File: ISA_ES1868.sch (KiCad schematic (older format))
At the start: 44 parts, among them J1 ISA BUS, J1 LINE, J2 MIC, J3 Joystick/MIDI, J5 Wavetable, U1 L78L05_TO92, U2 74LS138, U4 93LC66, Y1 14.318Mhz

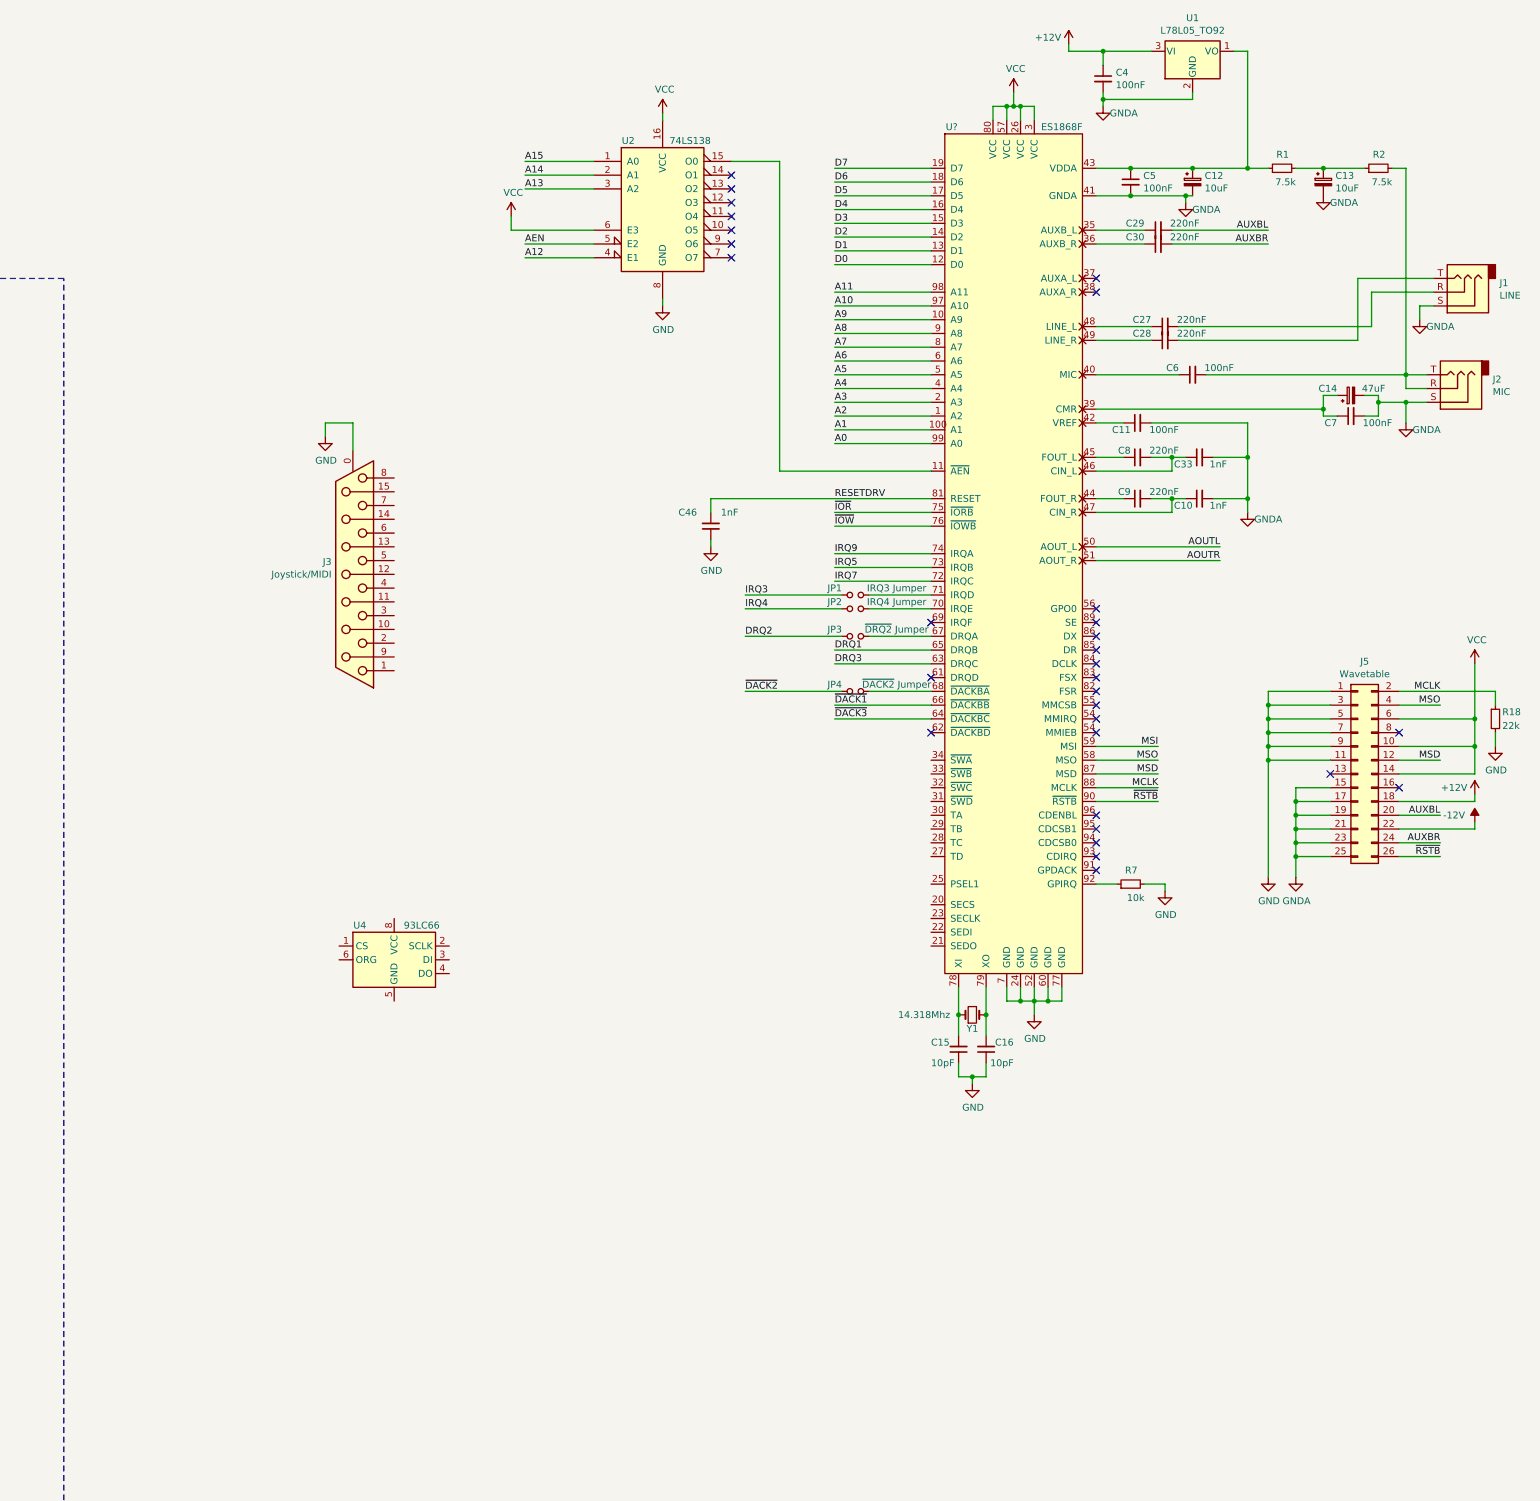
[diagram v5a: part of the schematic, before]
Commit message: Partial schematic for ESS chip done
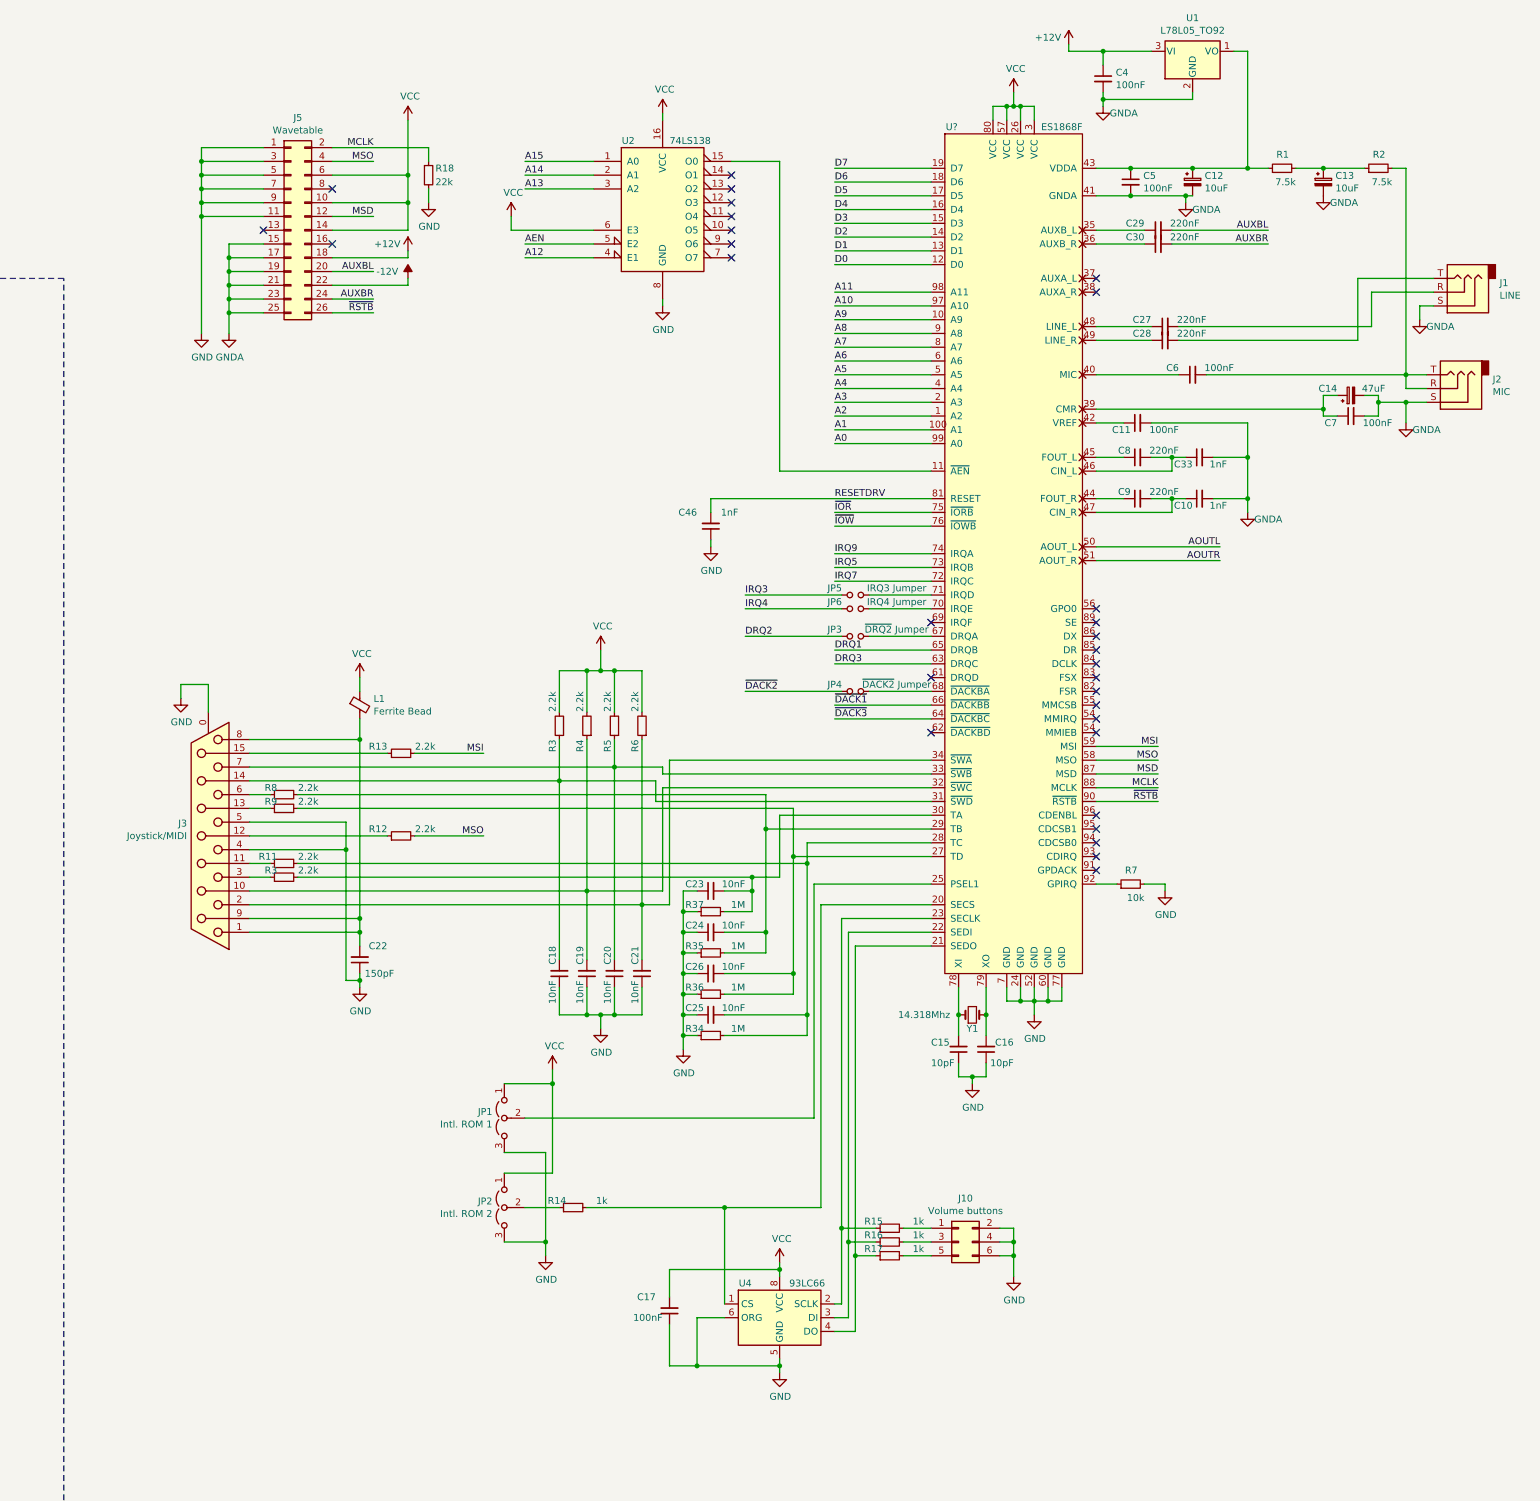
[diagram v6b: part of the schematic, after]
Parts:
- added C17: 100nF, Capacitor_THT:C_Disc_D6.0mm_W2.5mm_P5.00mm, symbol Device:C_Small
- added C18, C19, C20, C21, C23, C24, C25, C26: 10nF, Capacitor_THT:C_Disc_D6.0mm_W2.5mm_P5.00mm, symbol Device:C_Small
- added C22: 150pF, Capacitor_THT:C_Disc_D6.0mm_W2.5mm_P5.00mm, symbol Device:C_Small
- added J10: Volume buttons, symbol Connector_Generic:Conn_02x03_Odd_Even
- added JP1: Intl. ROM 1, symbol Jumper:Jumper_3_Open
- added JP2: Intl. ROM 2, symbol Jumper:Jumper_3_Open
- added L1: Ferrite Bead, symbol Device:Ferrite_Bead_Small
- added R11, R12, R13, R3 (x2), R4, R5, R6, R8, R9: 2.2k, symbol Device:R_Small
- added R14, R15, R16, R17: 1k, symbol Device:R_Small
- added R34, R35, R36, R37: 1M, symbol Device:R_Small
- renumbered JP1 to JP5, JP2 to JP6
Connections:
- net GND: now also J3.4, J3.5, U4.5 (GND), U4.6 (ORG), C17.1, C18.1, C19.1, C20.1, C21.1, C22.1, C23.1, C24.1, C25.1, C26.1, J10.2 (Pin_2), J10.4 (Pin_4), J10.6 (Pin_6), JP1.3 (B), JP2.3 (B), R34.1, R35.1, R36.1, R37.1
- net MSI: now also R13.2
- net MSO: now also R12.2
- net VCC: now also U4.8 (VCC), C17.2, JP1.1 (A), JP2.1 (A), L1.1, R3.2, R4.2, R5.2, R6.2
- net at U?.20 (SECS): now also U4.1 (CS), R14.2
- net at U?.21 (SEDO): now also U4.4 (DO), R17.1
- net at U?.22 (SEDI): now also U4.3 (DI), R16.1
- net at U?.23 (SECLK): now also U4.2 (SCLK), R15.1
- net at U?.25 (PSEL1): now also JP1.2 (C)
- net at U?.27 (TD): now also C26.2, R36.2, R9.2
- net at U?.28 (TC): now also C25.2, R11.2, R34.2
- net at U?.29 (TB): now also C24.2, R35.2, R8.2
- net at U?.30 (TA): now also C23.2, R3.2, R37.2
- net at U?.31 (~SWD): now also J3.14 (P14), C18.2, R3.1
- net at U?.32 (~SWC): now also J3.10 (P10), C19.2, R4.1
- net at U?.33 (~SWB): now also J3.7, C20.2, R5.1
- net at U?.34 (~SWA): now also J3.2, C21.2, R6.1
- net at J3.1: now also J3.8, J3.9 (P9), C22.2, L1.2
- net at J3.11 (P111): now also R11.1
- net at J3.12 (P12): now also R12.1
- net at J3.13 (P13): now also R9.1
- net at J3.15 (P15): now also R13.1
- net at J3.3: now also R3.1
- net at J3.6: now also R8.1
- new net: JP2.2 (C), R14.1
- new net: J10.1 (Pin_1), R15.2
- new net: J10.3 (Pin_3), R16.2
- new net: J10.5 (Pin_5), R17.2
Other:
- moved on the sheet: J3, J5, R18, U4

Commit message: Completed the schematics
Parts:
- added C2, C3, C41, C?: 100nF, Capacitor_THT:C_Disc_D6.0mm_W2.5mm_P5.00mm, symbol Device:C_Small
- added C34, C35: 470uF, Capacitor_THT:CP_Radial_D5.0mm_P2.50mm, symbol Device:CP_Small
- added C36, C37: 10uF, Capacitor_THT:C_Disc_D6.0mm_W2.5mm_P5.00mm, symbol Device:C_Small
- added C38, C39: 10nF, Capacitor_THT:C_Disc_D6.0mm_W2.5mm_P5.00mm, symbol Device:C_Small
- added C42: 100uF, Capacitor_THT:CP_Radial_D5.0mm_P2.50mm, symbol Device:CP_Small
- added C43: 47uF, Capacitor_THT:CP_Radial_D5.0mm_P2.50mm, symbol Device:CP_Small
- added C47, C48: 220nF, Capacitor_THT:C_Disc_D6.0mm_W2.5mm_P5.00mm, symbol Device:C_Small
- added J7: SPKR OUT, symbol Connector:AudioJack3
- added J8: LINE OUT, symbol Connector:AudioJack3
- added L2: Ferrite Bead, symbol Device:Ferrite_Bead_Small
- added R22, R23: 33k, symbol Device:R_Small
- added R24, R25, R26, R27: 820k, symbol Device:R_Small
- added R28, R?: 2.7, symbol Device:R_Small
- added R30, R31: 15k, symbol Device:R_Small
- added R32, R33: 10k, symbol Device:R_Small
- added U7: LM1877, symbol Amplifier_Audio:LM1877
- J1: value LINE -> LINE IN
- gave numbers to parts that had none: 7
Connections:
- net +12V: now also L2.1
- net AOUTL: now also C37.1, R31.1
- net AOUTR: now also C36.1, R30.1
- net GND: now also C2.2, C3.2
- net GNDA: now also C42.2, C43.2, J7.S, J8.S, R28.1, R32.2, R33.2, R?.1, U7.10 (GND), U7.11 (GND), U7.12 (GND), U7.3 (GND), U7.4 (GND), U7.5 (GND)
- net VCC: now also C2.1, C3.1
- new net: C37.2, J8.R
- new net: C36.2, J8.T
- new net: C42.1, L2.2, U7.14 (V+)
- new net: C47.1, R30.2, R32.1
- new net: C48.1, R31.2, R33.1
- new net: C47.2, R22.1
- new net: C48.2, R23.1
- new net: R22.2, R24.1, R25.1, U7.7 (-)
- new net: R23.2, R26.1, R27.1, U7.8 (-)
- new net: C43.1, U7.1 (BIAS), U7.6 (+), U7.9 (+)
- new net: C34.1, C38.2, C41.2, R25.2, U7.2
- new net: C35.1, C39.2, C?.2, R26.2, U7.13
- new net: C38.1, R24.2
- new net: C39.1, R27.2
- new net: C41.1, R28.2
- new net: C?.1, R?.2
- new net: C34.2, J7.T
- new net: C35.2, J7.R
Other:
- moved on the sheet: C10, C11, C12, C13, C14, C15, C16, C17, C18, C19, C20, C21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

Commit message: Complete schematic
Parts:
- added L3: Ferrite Bead, Inductor_THT:L_Axial_L5.3mm_D2.2mm_P7.62mm_Horizontal_Vishay_IM-1, symbol Device:Ferrite_Bead_Small
- J10: footprint (none) -> Connector_PinHeader_2.54mm:PinHeader_2x03_P2.54mm_Vertical
- J3: footprint (none) -> Connector_Dsub:DSUB-15_Female_Horizontal_P2.77x2.84mm_EdgePinOffset4.94mm_Housed_MountingHolesOffset7.48mm
- J5: footprint (none) -> Connector_PinHeader_2.54mm:PinHeader_2x13_P2.54mm_Vertical
- L1, L2: footprint (none) -> Inductor_THT:L_Axial_L5.3mm_D2.2mm_P7.62mm_Horizontal_Vishay_IM-1
- U2: footprint (none) -> Package_DIP:DIP-16_W7.62mm_LongPads
- U4: footprint (none) -> Package_DIP:DIP-8_W7.62mm_LongPads
- gave numbers to parts that had none: 3
- renumbered C31 to C50, C32 to C51, C33 to C52, C34 to C53, C35 to C54, C36 to C55, J1 to J11, R3 to R10
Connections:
- net GND: now also L3.1
- net GNDA: now also L3.2
